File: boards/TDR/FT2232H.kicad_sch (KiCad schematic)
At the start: 33 parts, among them U11 93LCxxBxxOT, U12 FT2232HL, U13 MIC5504-3.3YM5, Y1 12MHz

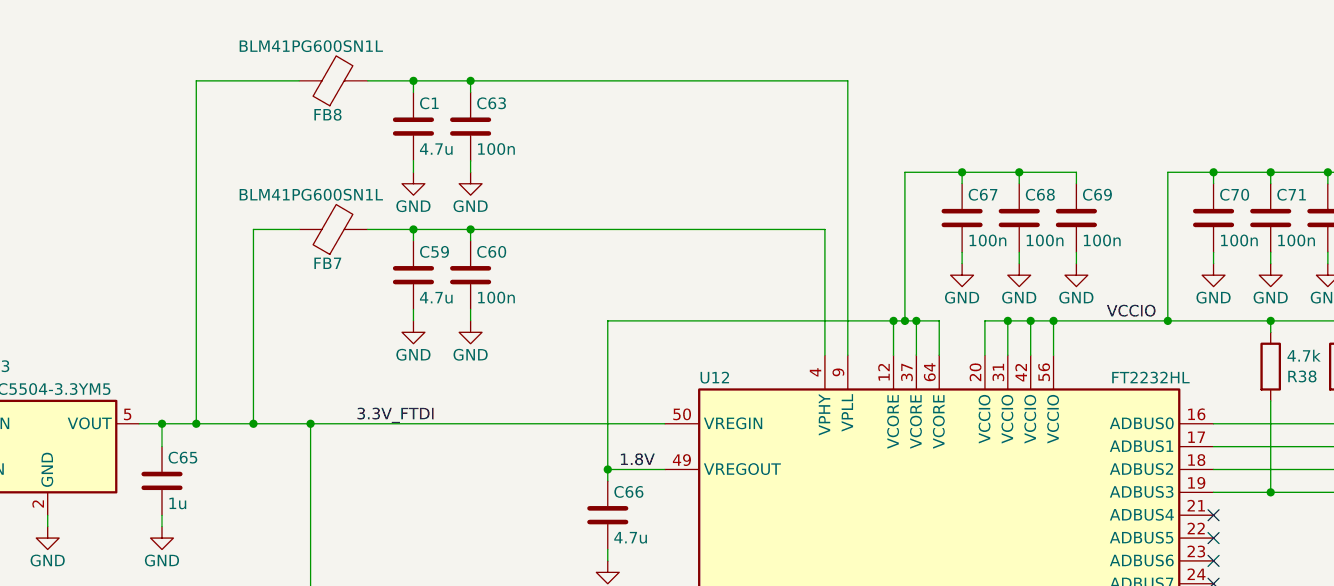
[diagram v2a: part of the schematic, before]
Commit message: connect fpga vccio to 3.3V, add decoupling, route some tracks
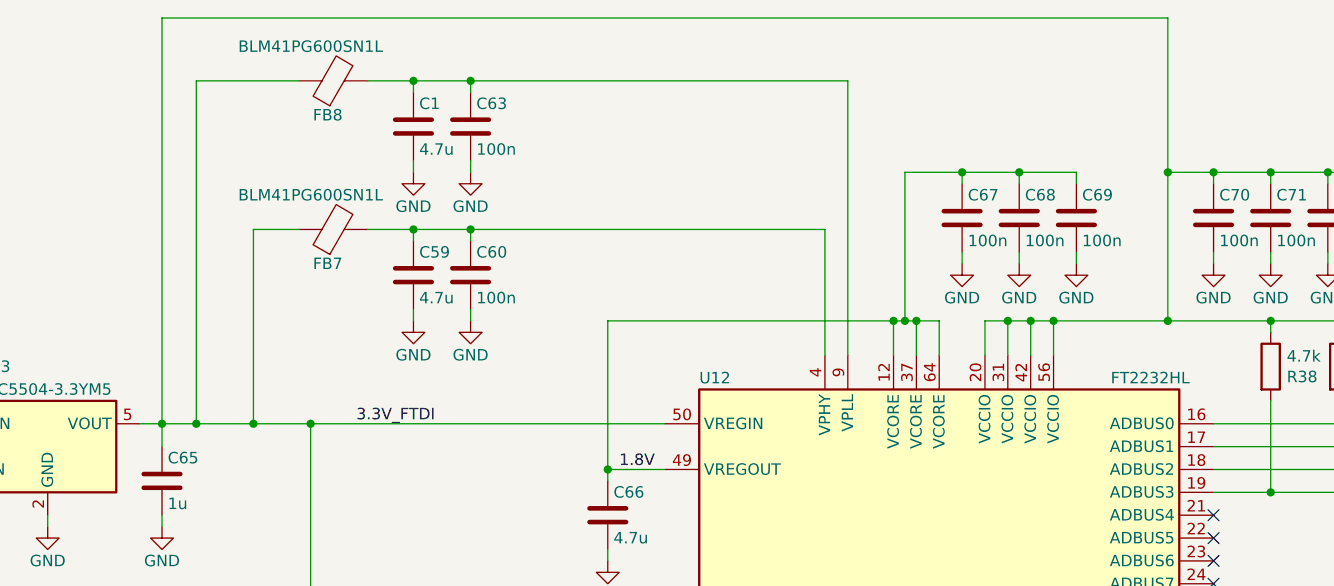
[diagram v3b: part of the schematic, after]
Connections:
- net VCCIO is gone; now on net 3.3V_FTDI: C70.1, C71.1, C72.1, C73.1, R38.1, R39.1, R40.1, U12.20 (VCCIO), U12.31 (VCCIO), U12.42 (VCCIO), U12.56 (VCCIO)
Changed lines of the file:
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@@
   (junction (at 179.07 46.99) (diameter 0) (color 0 0 0 0))
   (junction (at 181.61 46.99) (diameter 0) (color 0 0 0 0))
+  (junction (at 194.31 30.48) (diameter 0) (color 0 0 0 0))
   (junction (at 194.31 46.99) (diameter 0) (color 0 0 0 0))
   (junction (at 199.39 30.48) (diameter 0) (color 0 0 0 0))
@@
   (junction (at 220.98 60.96) (diameter 0) (color 0 0 0 0))
   (junction (at 228.6 58.42) (diameter 0) (color 0 0 0 0))
+  (no_connect (at 199.39 139.7))
+  (no_connect (at 199.39 86.36))
+  (no_connect (at 199.39 96.52))
+  (no_connect (at 199.39 71.12))
+  (no_connect (at 199.39 91.44))
+  (no_connect (at 199.39 142.24))
+  (no_connect (at 199.39 144.78))
+  (no_connect (at 199.39 68.58))
+  (no_connect (at 199.39 99.06))
+  (no_connect (at 199.39 149.86))
+  (no_connect (at 199.39 93.98))
+  (no_connect (at 199.39 81.28))
+  (no_connect (at 199.39 73.66))
   (no_connect (at 199.39 88.9))
-  (no_connect (at 199.39 96.52))
-  (no_connect (at 199.39 142.24))
-  (no_connect (at 199.39 68.58))
-  (no_connect (at 199.39 73.66))
-  (no_connect (at 199.39 91.44))
-  (no_connect (at 199.39 144.78))
-  (no_connect (at 199.39 139.7))
+  (no_connect (at 199.39 152.4))
   (no_connect (at 199.39 83.82))
   (no_connect (at 199.39 76.2))
-  (no_connect (at 199.39 99.06))
-  (no_connect (at 199.39 81.28))
-  (no_connect (at 199.39 152.4))
-  (no_connect (at 199.39 71.12))
-  (no_connect (at 199.39 93.98))
-  (no_connect (at 199.39 86.36))
-  (no_connect (at 199.39 149.86))
   (wire (pts (xy 38.1 58.42) (xy 46.99 58.42))
     (stroke (width 0) (type solid) (color 0 0 0 0))
@@
     (stroke (width 0) (type solid) (color 0 0 0 0))
   )
+  (wire (pts (xy 82.55 13.335) (xy 194.31 13.335))
+    (stroke (width 0) (type solid) (color 0 0 0 0))
+  )
+  (wire (pts (xy 82.55 58.42) (xy 82.55 13.335))
+    (stroke (width 0) (type solid) (color 0 0 0 0))
+  )
   (wire (pts (xy 82.55 58.42) (xy 82.55 60.96))
     (stroke (width 0) (type solid) (color 0 0 0 0))
@@
   )
   (wire (pts (xy 184.15 39.37) (xy 184.15 40.64))
+    (stroke (width 0) (type solid) (color 0 0 0 0))
+  )
+  (wire (pts (xy 194.31 13.335) (xy 194.31 30.48))
     (stroke (width 0) (type solid) (color 0 0 0 0))
   )
@@
     (effects (font (size 1.27 1.27)) (justify left bottom))
   )
-  (label "VCCIO" (at 193.04 46.99 180)
-    (effects (font (size 1.27 1.27)) (justify right bottom))
-  )
   (hierarchical_label "5V_INPUT" (shape input) (at 38.1 58.42 180)

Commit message: hopefully PCB is done
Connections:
- net 3.3V_FTDI: now also C58.2, R32.1, R34.1, R35.1, U11.6 (VCC)
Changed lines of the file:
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@@
   )
   (junction (at 46.99 58.42) (diameter 0) (color 0 0 0 0))
+  (junction (at 55.88 114.3) (diameter 0) (color 0 0 0 0))
   (junction (at 74.93 114.3) (diameter 0) (color 0 0 0 0))
   (junction (at 82.55 58.42) (diameter 0) (color 0 0 0 0))
   (junction (at 86.36 58.42) (diameter 0) (color 0 0 0 0))
+  (junction (at 89.535 58.42) (diameter 0) (color 0 0 0 0))
   (junction (at 90.17 114.3) (diameter 0) (color 0 0 0 0))
   (junction (at 90.17 132.08) (diameter 0) (color 0 0 0 0))
@@
     (stroke (width 0) (type solid) (color 0 0 0 0))
   )
+  (wire (pts (xy 55.88 100.33) (xy 55.88 114.3))
+    (stroke (width 0) (type solid) (color 0 0 0 0))
+  )
   (wire (pts (xy 55.88 114.3) (xy 74.93 114.3))
     (stroke (width 0) (type solid) (color 0 0 0 0))
@@
     (stroke (width 0) (type solid) (color 0 0 0 0))
   )
-  (wire (pts (xy 86.36 58.42) (xy 92.71 58.42))
+  (wire (pts (xy 86.36 58.42) (xy 89.535 58.42))
     (stroke (width 0) (type solid) (color 0 0 0 0))
   )
@@
     (stroke (width 0) (type solid) (color 0 0 0 0))
   )
+  (wire (pts (xy 89.535 58.42) (xy 89.535 100.33))
+    (stroke (width 0) (type solid) (color 0 0 0 0))
+  )
+  (wire (pts (xy 89.535 58.42) (xy 92.71 58.42))
+    (stroke (width 0) (type solid) (color 0 0 0 0))
+  )
+  (wire (pts (xy 89.535 100.33) (xy 55.88 100.33))
+    (stroke (width 0) (type solid) (color 0 0 0 0))
+  )
